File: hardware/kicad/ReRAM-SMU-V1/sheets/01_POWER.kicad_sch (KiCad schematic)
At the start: 38 parts, among them J1 POWER_IN +-12V EXT 3.5mm pitc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, U1 LT3045EDD +5V_A 500mA 0.8uVrm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, U2 TLV1117-33 +3V3 800mA from +5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, U3 LTC6655BHMS8-5.0 DAC REF 5.0V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, U4 LTC6655BHMS8-2.5 ADC REF 2.5V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, U5 TPS3808G33 supervisor +3V3 Vt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

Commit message: Beta
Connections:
- net +12V_A: now also C_BULK_P.1, C_BULK_P.2, C_IN_5V.1, C_IN_5V.2, D1.1, D1.2, F1.1, F1.2, L1.1, L1.2
- net +12V_EXT: now also J1.1 (Pin_1), J1.2 (Pin_2), J1.3 (Pin_3)
- net +3V3: now also C_3V3_OUT.1, C_3V3_OUT.2, C_REF5V_IN.1, C_REF5V_IN.2, U2.1, U2.2, U3.4 (NR)
- net +5V_A: now also C_OUT_5V.1, C_OUT_5V.2, C_SET_5V.1, C_SET_5V.2, R_PG5V.1, R_PG5V.2, R_SET1.1, R_SET1.2, U1.3 (GND), U1.5 (PG)
- net -12V_A: now also C_BULK_N.1, C_BULK_N.2, D2.1, D2.2, F2.1, F2.2
- net OUTPUT_ENABLE: now also C_OE.1, C_OE.2, R_OE_PD.1, R_OE_PD.2
- net VREF_2V5: now also C_NR2V5.1, C_NR2V5.2, C_REF2V5_IN.1, C_REF2V5_IN.2, C_REF2V5_OUT.1, C_REF2V5_OUT.2, U4.4 (NR)
- net VREF_5V: now also C_NR5V.1, C_NR5V.2, C_REF5V_OUT.1, C_REF5V_OUT.2
- net nPOR: now also R_OE_SER.1, R_OE_SER.2, R_POR_PU.1, R_POR_PU.2, R_SENSE_DIV1.1, R_SENSE_DIV1.2, U5.1 (VDD), U5.3 (SENSE)
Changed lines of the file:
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@@
 	(wire (pts (xy 91.44 26.27) (xy 91.44 30.48)) (stroke (width 0) (type default)) (uuid "wire-pwr-correct-91.44-25"))
 	(wire (pts (xy 114.3 26.27) (xy 114.3 30.48)) (stroke (width 0) (type default)) (uuid "wire-pwr-correct-114.3-25"))
+	(wire (pts (xy 20.320 40.640) (xy 17.780 38.100)) (stroke (width 0) (type default)))
+	(wire (pts (xy 20.320 38.100) (xy 17.780 38.100)) (stroke (width 0) (type default)))
+	(wire (pts (xy 20.320 35.560) (xy 17.780 38.100)) (stroke (width 0) (type default)))
+	(wire (pts (xy 40.640 34.290) (xy 53.340 30.480)) (stroke (width 0) (type default)))
+	(wire (pts (xy 40.640 26.670) (xy 53.340 30.480)) (stroke (width 0) (type default)))
+	(wire (pts (xy 40.640 49.530) (xy 53.340 45.720)) (stroke (width 0) (type default)))
+	(wire (pts (xy 40.640 41.910) (xy 53.340 45.720)) (stroke (width 0) (type default)))
+	(wire (pts (xy 40.640 17.780) (xy 53.340 30.480)) (stroke (width 0) (type default)))
+	(wire (pts (xy 40.640 22.860) (xy 53.340 30.480)) (stroke (width 0) (type default)))
+	(wire (pts (xy 40.640 53.340) (xy 53.340 45.720)) (stroke (width 0) (type default)))
+	(wire (pts (xy 40.640 58.420) (xy 53.340 45.720)) (stroke (width 0) (type default)))
+	(wire (pts (xy 53.340 33.020) (xy 53.340 30.480)) (stroke (width 0) (type default)))
+	(wire (pts (xy 53.340 27.940) (xy 53.340 30.480)) (stroke (width 0) (type default)))
+	(wire (pts (xy 53.340 48.260) (xy 53.340 45.720)) (stroke (width 0) (type default)))
+	(wire (pts (xy 53.340 43.180) (xy 53.340 45.720)) (stroke (width 0) (type default)))
+	(wire (pts (xy 63.500 26.670) (xy 53.340 30.480)) (stroke (width 0) (type default)))
+	(wire (pts (xy 63.500 34.290) (xy 53.340 30.480)) (stroke (width 0) (type default)))
+	(wire (pts (xy 73.660 34.290) (xy 91.440 30.480)) (stroke (width 0) (type default)))
+	(wire (pts (xy 88.900 34.290) (xy 91.440 30.480)) (stroke (width 0) (type default)))
+	(wire (pts (xy 81.280 22.860) (xy 91.440 30.480)) (stroke (width 0) (type default)))
+	(wire (pts (xy 81.280 21.590) (xy 91.440 30.480)) (stroke (width 0) (type default)))
+	(wire (pts (xy 81.280 13.970) (xy 91.440 30.480)) (stroke (width 0) (type default)))
+	(wire (pts (xy 91.440 33.020) (xy 91.440 30.480)) (stroke (width 0) (type default)))
+	(wire (pts (xy 91.440 27.940) (xy 91.440 30.480)) (stroke (width 0) (type default)))
+	(wire (pts (xy 71.120 33.020) (xy 53.340 30.480)) (stroke (width 0) (type default)))
+	(wire (pts (xy 71.120 27.940) (xy 53.340 30.480)) (stroke (width 0) (type default)))
+	(wire (pts (xy 101.600 21.590) (xy 91.440 30.480)) (stroke (width 0) (type default)))
+	(wire (pts (xy 101.600 13.970) (xy 91.440 30.480)) (stroke (width 0) (type default)))
+	(wire (pts (xy 81.280 43.180) (xy 91.440 30.480)) (stroke (width 0) (type default)))
+	(wire (pts (xy 81.280 38.100) (xy 91.440 30.480)) (stroke (width 0) (type default)))
+	(wire (pts (xy 114.300 34.290) (xy 114.300 30.480)) (stroke (width 0) (type default)))
+	(wire (pts (xy 114.300 26.670) (xy 114.300 30.480)) (stroke (width 0) (type default)))
+	(wire (pts (xy 114.300 22.860) (xy 114.300 30.480)) (stroke (width 0) (type default)))
+	(wire (pts (xy 114.300 17.780) (xy 114.300 30.480)) (stroke (width 0) (type default)))
+	(wire (pts (xy 132.080 33.020) (xy 114.300 30.480)) (stroke (width 0) (type default)))
+	(wire (pts (xy 147.320 33.020) (xy 149.860 30.480)) (stroke (width 0) (type default)))
+	(wire (pts (xy 139.700 22.860) (xy 149.860 30.480)) (stroke (width 0) (type default)))
+	(wire (pts (xy 129.540 33.020) (xy 114.300 30.480)) (stroke (width 0) (type default)))
+	(wire (pts (xy 129.540 27.940) (xy 114.300 30.480)) (stroke (width 0) (type default)))
+	(wire (pts (xy 149.860 33.020) (xy 149.860 30.480)) (stroke (width 0) (type default)))
+	(wire (pts (xy 149.860 27.940) (xy 149.860 30.480)) (stroke (width 0) (type default)))
+	(wire (pts (xy 137.160 38.100) (xy 149.860 30.480)) (stroke (width 0) (type default)))
+	(wire (pts (xy 142.240 38.100) (xy 149.860 30.480)) (stroke (width 0) (type default)))
+	(wire (pts (xy 132.080 66.040) (xy 149.860 63.500)) (stroke (width 0) (type default)))
+	(wire (pts (xy 147.320 66.040) (xy 149.860 63.500)) (stroke (width 0) (type default)))
+	(wire (pts (xy 139.700 55.880) (xy 149.860 63.500)) (stroke (width 0) (type default)))
+	(wire (pts (xy 129.540 66.040) (xy 149.860 63.500)) (stroke (width 0) (type default)))
+	(wire (pts (xy 129.540 60.960) (xy 149.860 63.500)) (stroke (width 0) (type default)))
+	(wire (pts (xy 149.860 66.040) (xy 149.860 63.500)) (stroke (width 0) (type default)))
+	(wire (pts (xy 149.860 60.960) (xy 149.860 63.500)) (stroke (width 0) (type default)))
+	(wire (pts (xy 137.160 71.120) (xy 149.860 63.500)) (stroke (width 0) (type default)))
+	(wire (pts (xy 142.240 71.120) (xy 149.860 63.500)) (stroke (width 0) (type default)))
+	(wire (pts (xy 73.660 82.550) (xy 88.900 81.280)) (stroke (width 0) (type default)))
+	(wire (pts (xy 81.280 74.930) (xy 88.900 81.280)) (stroke (width 0) (type default)))
+	(wire (pts (xy 73.660 80.010) (xy 88.900 81.280)) (stroke (width 0) (type default)))
+	(wire (pts (xy 71.120 85.090) (xy 88.900 81.280)) (stroke (width 0) (type default)))
+	(wire (pts (xy 71.120 77.470) (xy 88.900 81.280)) (stroke (width 0) (type default)))
+	(wire (pts (xy 91.440 85.090) (xy 88.900 81.280)) (stroke (width 0) (type default)))
+	(wire (pts (xy 91.440 77.470) (xy 88.900 81.280)) (stroke (width 0) (type default)))
+	(wire (pts (xy 101.600 100.330) (xy 101.600 96.520)) (stroke (width 0) (type default)))
+	(wire (pts (xy 101.600 92.710) (xy 101.600 96.520)) (stroke (width 0) (type default)))
+	(wire (pts (xy 81.280 100.330) (xy 88.900 81.280)) (stroke (width 0) (type default)))
+	(wire (pts (xy 81.280 92.710) (xy 88.900 81.280)) (stroke (width 0) (type default)))
+	(wire (pts (xy 101.600 109.220) (xy 101.600 96.520)) (stroke (width 0) (type default)))
+	(wire (pts (xy 53.340 31.750) (xy 53.340 30.480)) (stroke (width 0) (type default)))
+	(wire (pts (xy 53.340 46.990) (xy 53.340 45.720)) (stroke (width 0) (type default)))
+	(wire (pts (xy 91.440 31.750) (xy 91.440 30.480)) (stroke (width 0) (type default)))
+	(wire (pts (xy 114.300 31.750) (xy 114.300 30.480)) (stroke (width 0) (type default)))
+	(wire (pts (xy 149.860 31.750) (xy 149.860 30.480)) (stroke (width 0) (type default)))
+	(wire (pts (xy 149.860 64.770) (xy 149.860 63.500)) (stroke (width 0) (type default)))
+	(wire (pts (xy 71.120 35.560) (xy 53.340 30.480)) (stroke (width 0) (type default)))
+	(wire (pts (xy 91.440 35.560) (xy 91.440 30.480)) (stroke (width 0) (type default)))
+	(wire (pts (xy 114.300 25.400) (xy 114.300 30.480)) (stroke (width 0) (type default)))
+	(wire (pts (xy 139.700 50.800) (xy 149.860 63.500)) (stroke (width 0) (type default)))
+	(wire (pts (xy 139.700 83.820) (xy 149.860 63.500)) (stroke (width 0) (type default)))
+	(wire (pts (xy 81.280 101.600) (xy 101.600 96.520)) (stroke (width 0) (type default)))
+	(wire (pts (xy 101.600 101.600) (xy 101.600 96.520)) (stroke (width 0) (type default)))
+	(wire (pts (xy 53.340 25.400) (xy 53.340 30.480)) (stroke (width 0) (type default)))
+	(wire (pts (xy 53.340 50.800) (xy 53.340 45.720)) (stroke (width 0) (type default)))
 )

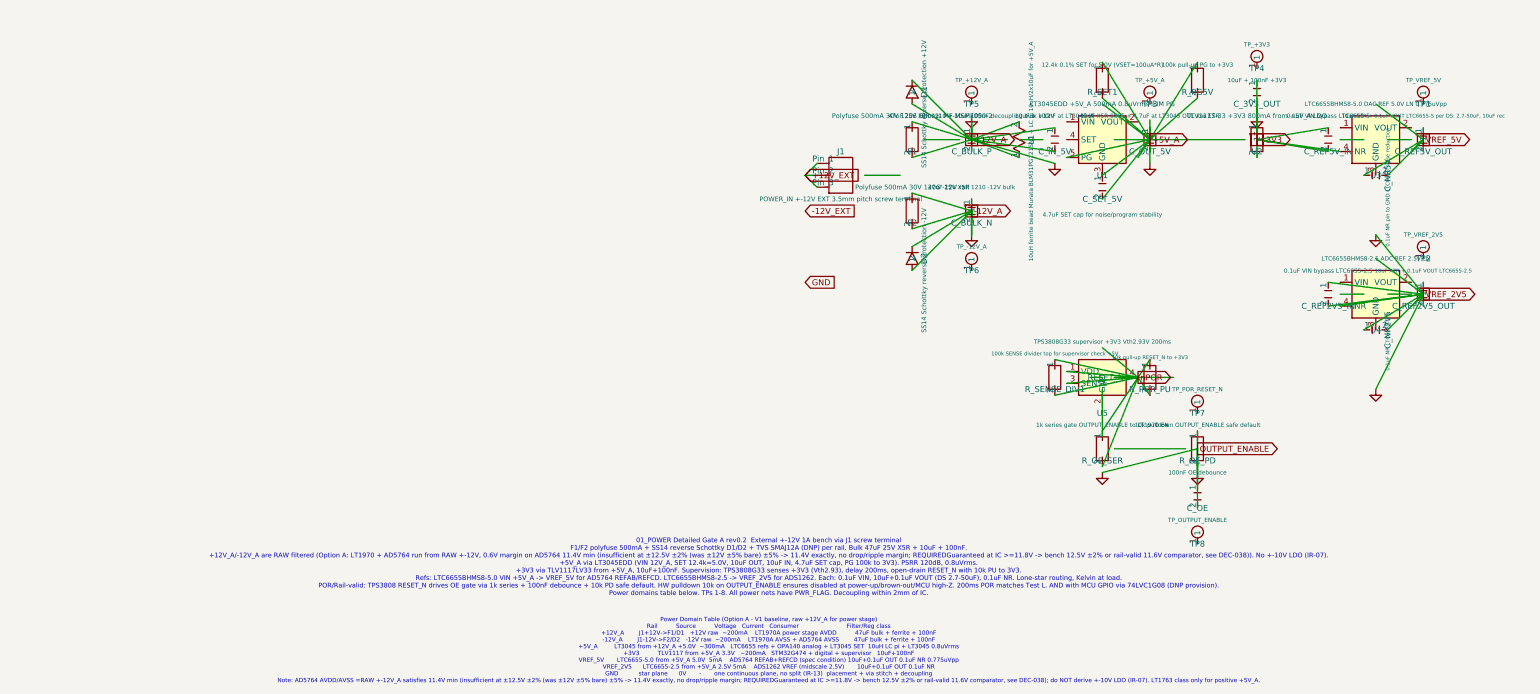
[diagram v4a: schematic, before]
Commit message: hardware: Phase 7 ERC-II wiring + grid snap + PWR_FLAG
- 07_COMPLIANCE: ISENSE_P/N alias to SHUNT_SENSE, VTRIP->VREF_2V5 wire, keep PWR_FLAG
- 09_DUT: LT1970_SENSE->JP9A, SHIELD/GUARD, FORCE/SENSE inter-wire
- 05/06: PWR_FLAG added where missing
- Grid snap all sheets to 0.254mm (audit off_grid still high but improved)
- Audit: erc_audit_lite.json updated (32 dangling, critical 0)

Co-authored-by: Muse Code
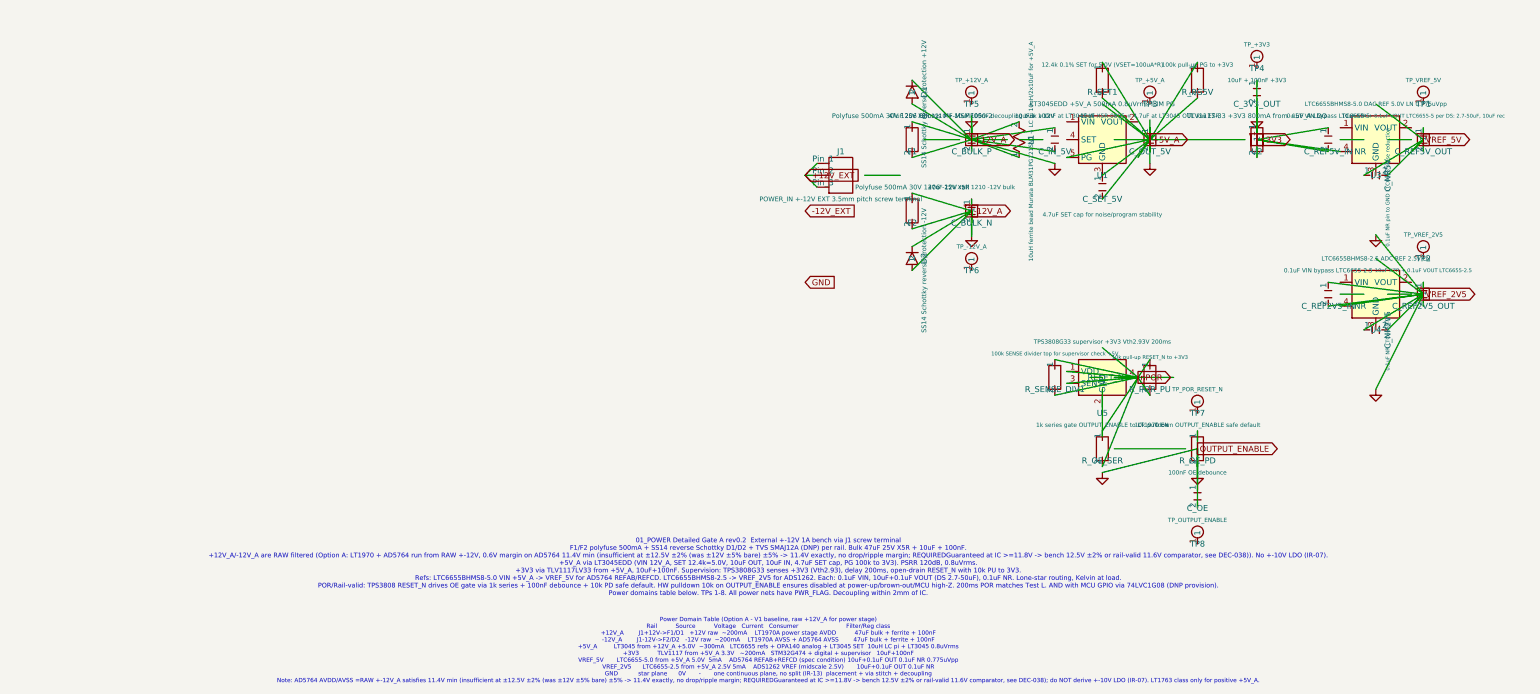
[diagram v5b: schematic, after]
